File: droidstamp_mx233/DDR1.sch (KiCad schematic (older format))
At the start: 16 parts, among them U2 MT46V32M16TG

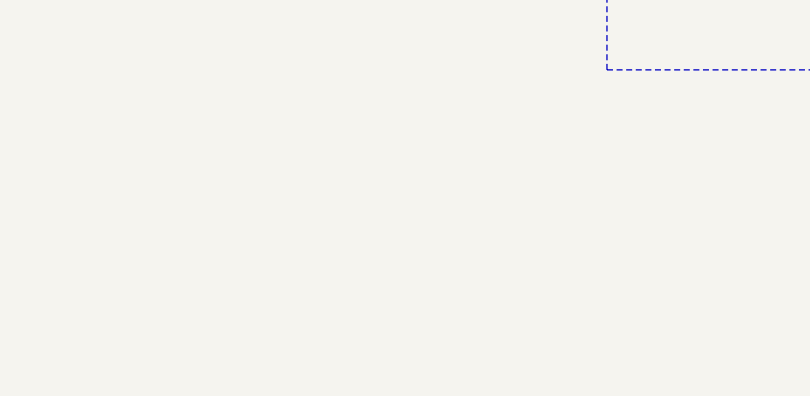
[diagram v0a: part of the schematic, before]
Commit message: TODO file added
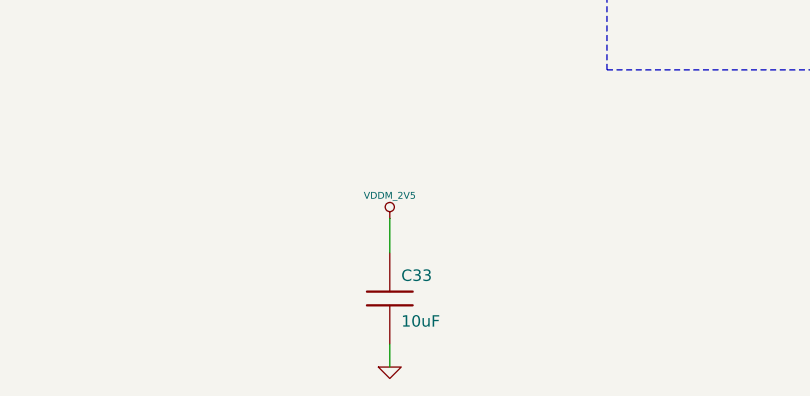
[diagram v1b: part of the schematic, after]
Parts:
- added C33: 10uF, SM1206, symbol C
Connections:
- wire segments 122 -> 124
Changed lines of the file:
@@
-EESchema Schematic File Version 2  date mié 12 sep 2012 20:12:14 COT
+EESchema Schematic File Version 2  date Wed 03 Oct 2012 07:36:32 PM COT
 LIBS:con-jack
 LIBS:adm3101e
@@
 EELAYER 25  0
 EELAYER END
-$Descr A4 11700 8267
+$Descr A4 11693 8268
 encoding utf-8
-Sheet 4 5
+Sheet 3 5
 Title ""
-Date "13 sep 2012"
+Date "4 oct 2012"
 Rev ""
 Comp ""
@@
 	5850 3800 7250 3800
 $Comp
-L VDDM_2V5 #PWR094
+L VDDM_2V5 #PWR88
 U 1 1 4D7E6BF9
 P 6000 3900
-F 0 "#PWR094" H 6000 4000 30  0001 C CNN
+F 0 "#PWR88" H 6000 4000 30  0001 C CNN
 F 1 "VDDM_2V5" H 5950 3950 30  0000 C CNN
 	1    6000 3900
@@
 $EndComp
 $Comp
-L GND #PWR095
+L GND #PWR87
 U 1 1 4D418353
 P 5850 4500
-F 0 "#PWR095" H 5850 4500 30  0001 C CNN
+F 0 "#PWR87" H 5850 4500 30  0001 C CNN
 F 1 "GND" H 5850 4430 30  0001 C CNN
 	1    5850 4500
@@
 DDR_CKE
 $Comp
-L GND #PWR096
+L GND #PWR95
 U 1 1 4D417AF1
 P 10800 2750
-F 0 "#PWR096" H 10800 2750 30  0001 C CNN
+F 0 "#PWR95" H 10800 2750 30  0001 C CNN
 F 1 "GND" H 10800 2680 30  0001 C CNN
 	1    10800 2750
@@
 $EndComp
 $Comp
-L VDDM_2V5 #PWR097
+L VDDM_2V5 #PWR94
 U 1 1 4D417ACD
 P 10800 1450
-F 0 "#PWR097" H 10800 1550 30  0001 C CNN
+F 0 "#PWR94" H 10800 1550 30  0001 C CNN
 F 1 "VDDM_2V5" H 10800 1550 30  0000 C CNN
 	1    10800 1450
@@
 $EndComp
 $Comp
-L VDDM_2V5 #PWR098
+L VDDM_2V5 #PWR89
 U 1 1 4D4179A4
 P 7250 800
-F 0 "#PWR098" H 7250 900 30  0001 C CNN
+F 0 "#PWR89" H 7250 900 30  0001 C CNN
 F 1 "VDDM_2V5" H 7250 900 30  0000 C CNN
 	1    7250 800
@@
 $EndComp
 $Comp
-L VDDM_2V5 #PWR099
+L VDDM_2V5 #PWR93
 U 1 1 4D417999
 P 10200 800
-F 0 "#PWR099" H 10200 900 30  0001 C CNN
+F 0 "#PWR93" H 10200 900 30  0001 C CNN
 F 1 "VDDM_2V5" H 10200 900 30  0000 C CNN
 	1    10200 800
@@
 $EndComp
 $Comp
-L GND #PWR0100
+L GND #PWR90
 U 1 1 4D41792B
 P 7550 1500
-F 0 "#PWR0100" H 7550 1500 30  0001 C CNN
+F 0 "#PWR90" H 7550 1500 30  0001 C CNN
 F 1 "GND" H 7550 1430 30  0001 C CNN
 	1    7550 1500
@@
 $EndComp
 $Comp
-L GND #PWR0101
+L GND #PWR92
 U 1 1 4D417882
 P 9600 1500
-F 0 "#PWR0101" H 9600 1500 30  0001 C CNN
+F 0 "#PWR92" H 9600 1500 30  0001 C CNN
 F 1 "GND" H 9600 1430 30  0001 C CNN
 	1    9600 1500
@@
 DDR_WEN
 $Comp
-L GND #PWR0102
+L GND #PWR91
 U 1 1 4D319D50
 P 8300 5050
-F 0 "#PWR0102" H 8300 5050 30  0001 C CNN
+F 0 "#PWR91" H 8300 5050 30  0001 C CNN
 F 1 "GND" H 8300 4980 30  0001 C CNN
 	1    8300 5050
@@
 	1    0    0    -1
 $EndComp
+$Comp
+L C C33
+U 1 1 506CE7F9
+P 4800 6300
+F 0 "C33" H 4850 6400 50  0000 L CNN
+F 1 "10uF" H 4850 6200 50  0000 L CNN
+F 2 "SM1206" H 4800 6300 60  0001 C CNN
+	1    4800 6300
+	1    0    0    -1
+$EndComp
+Wire Wire Line
+	4800 6500 4800 6600
+$Comp
+L GND #PWR86
+U 1 1 506CE824
+P 4800 6600
+F 0 "#PWR86" H 4800 6600 30  0001 C CNN
+F 1 "GND" H 4800 6530 30  0001 C CNN
+	1    4800 6600
+	1    0    0    -1
+$EndComp
+Wire Wire Line
+	4800 5950 4800 6100
+$Comp
+L VDDM_2V5 #PWR85
+U 1 1 506CE82B
+P 4800 5950
+F 0 "#PWR85" H 4800 6050 30  0001 C CNN
+F 1 "VDDM_2V5" H 4800 6050 30  0000 C CNN
+	1    4800 5950
+	1    0    0    -1
+$EndComp
